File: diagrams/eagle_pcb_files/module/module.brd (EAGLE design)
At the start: 37.5 x 29.7 mm, 3 parts

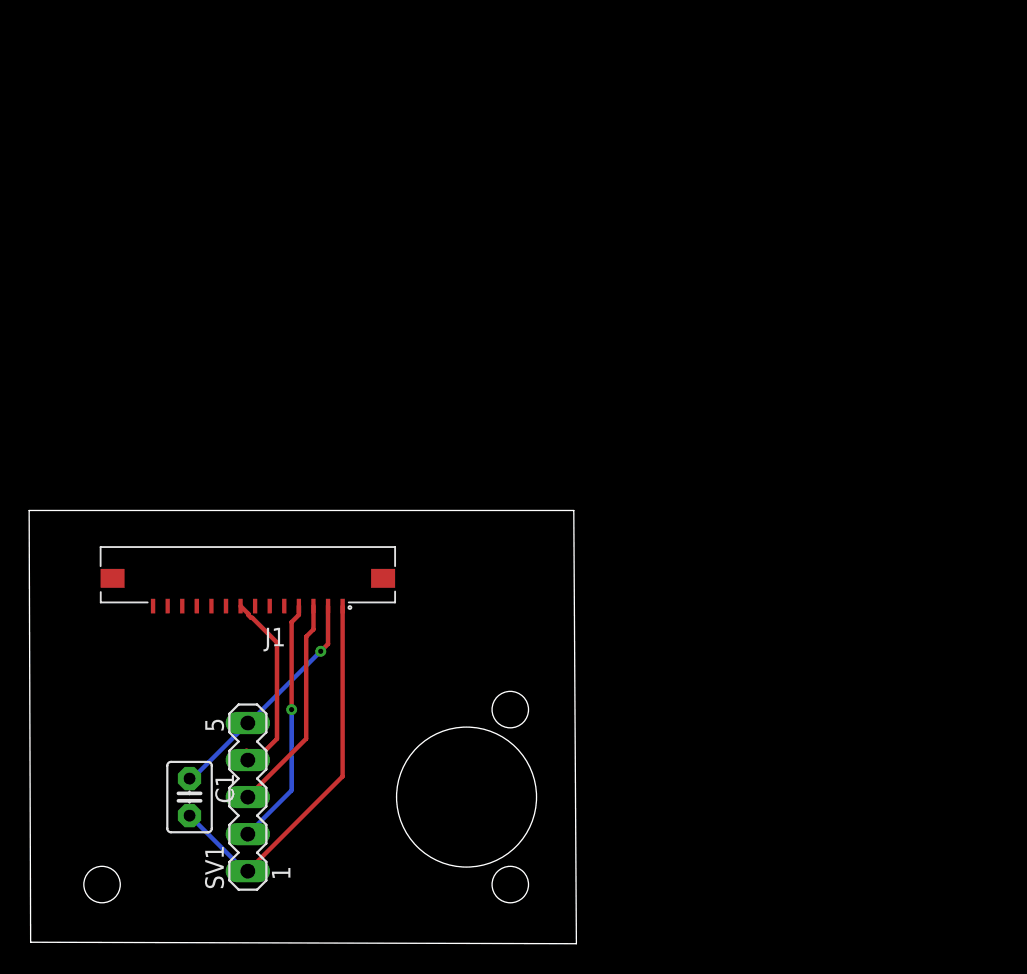
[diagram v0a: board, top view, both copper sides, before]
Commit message: small fixes, 100pF -> 100nF, tht cap to smd cap, mounting holes, round dimension, one sided instead of two sided, gnd plane
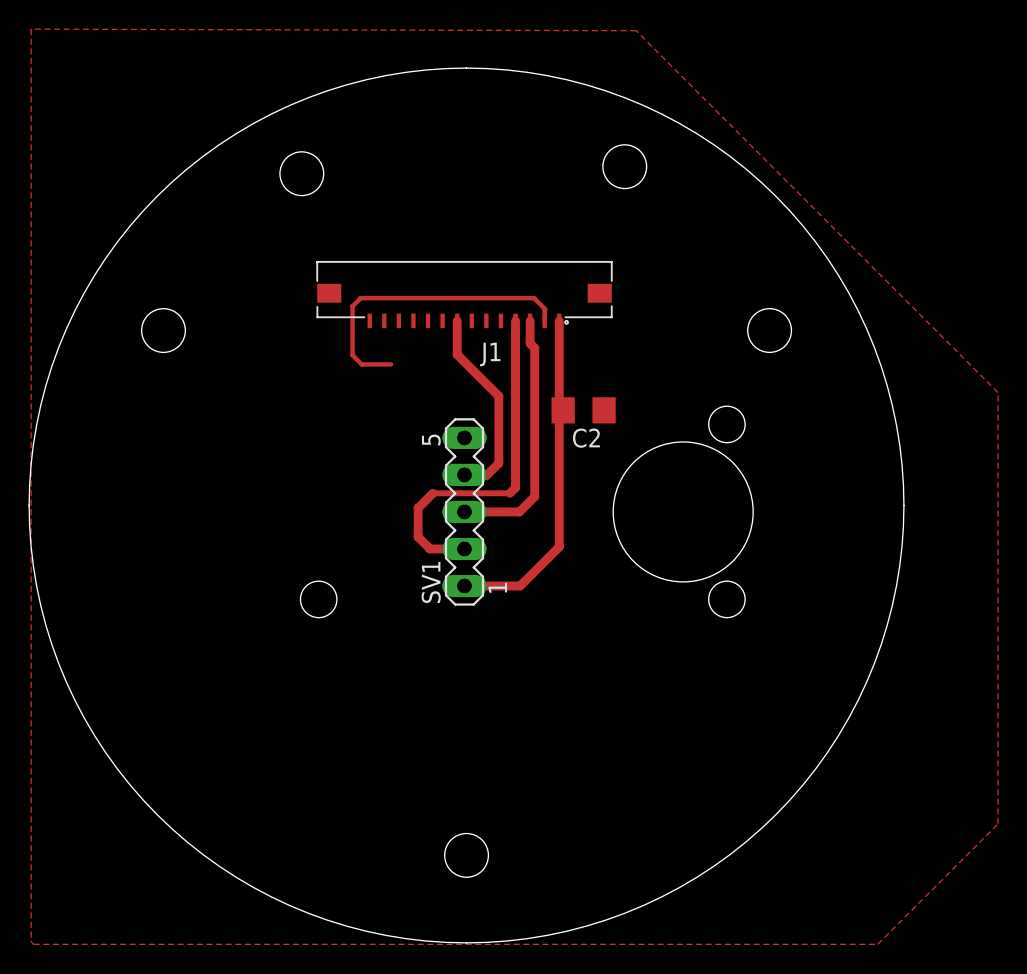
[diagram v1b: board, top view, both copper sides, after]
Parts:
- removed C1: 100pF, capacitor-wima:C2.5-3
- added C2: 100nF, eagle-ltspice:C1206
- moved J1 24.6 mm to (39.9, 44.6)
- moved SV1 24.6 mm to (39.9, 29.6)
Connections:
- net N$3 renamed SCL
- net N$4 renamed SDA
- net N$5 renamed INT
- removed net N$1: C1.2, J1.1, SV1.1
- removed net N$2: C1.1, J1.2, SV1.5
- new net GND: C2.1, J1.2, SV1.5
- new net VCC: C2.2, J1.1, SV1.1
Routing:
- net N$1: track 26.5 -> 0.00 mm
- net VCC: track 0.00 -> 23.4 mm
- net GND: track 0.00 -> 20.8 mm
- net N$2: track 15.9 -> 0.00 mm, vias 1 -> 0
- net SDA: track 17.1 -> 24.2 mm, vias 1 -> 0
- net SCL: track 15.0 -> 17.4 mm
- added copper zone on layer 1, net GND
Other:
- board size 37.5 x 29.7 mm -> 60 x 60 mm

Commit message: Some features added
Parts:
- moved C2 24.5 mm to (42.4, 12.6), turned to 0 degrees
- moved SV1 7.56 mm to (40.0, 22.0)
- moved J1 6.56 mm to (40.0, 38.0)
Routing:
- net VCC: track 23.4 -> 28.4 mm
- net INT: track 13.7 -> 14.7 mm
- net SCL: track 17.4 -> 18.4 mm
- net SDA: track 24.2 -> 25.2 mm
